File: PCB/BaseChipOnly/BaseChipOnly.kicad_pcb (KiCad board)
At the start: 2 copper layers, 39.1 x 68.8 mm, 31 parts, among them J1 Barrel_Jack_Connector, J2 Morsetto, J3 ESP32_PROG_1x6, U1 ESP32-WROOM-32U, U4 LM2596S-ADJ

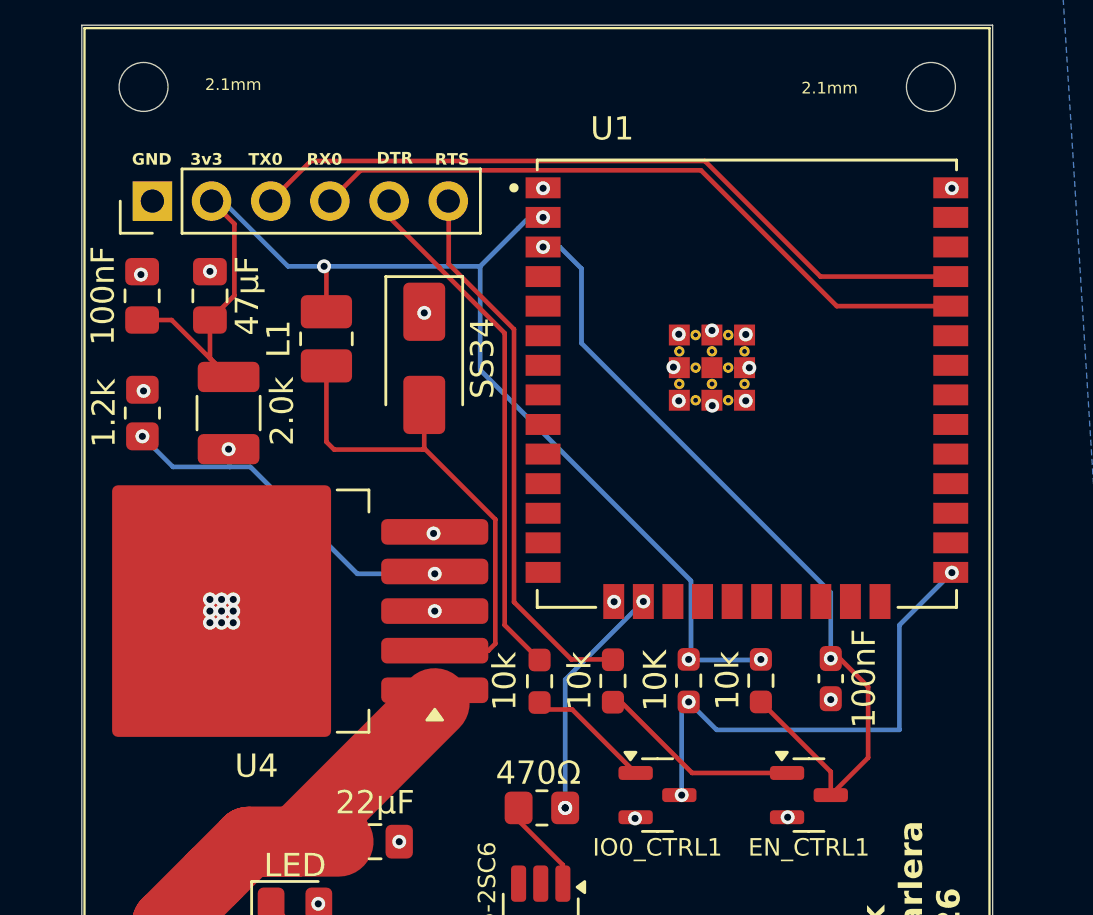
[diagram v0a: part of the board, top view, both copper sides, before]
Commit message: chore: update 3D models and PCB layout
Replace vaso/tappo STLs with new revisions (BaseVaso, Foglia, TasselloFissaggioPCB, VasoGiusto); minor kicad_pcb update.

Co-Authored-By: Claude Sonnet 5 <noreply@anthropic.com>
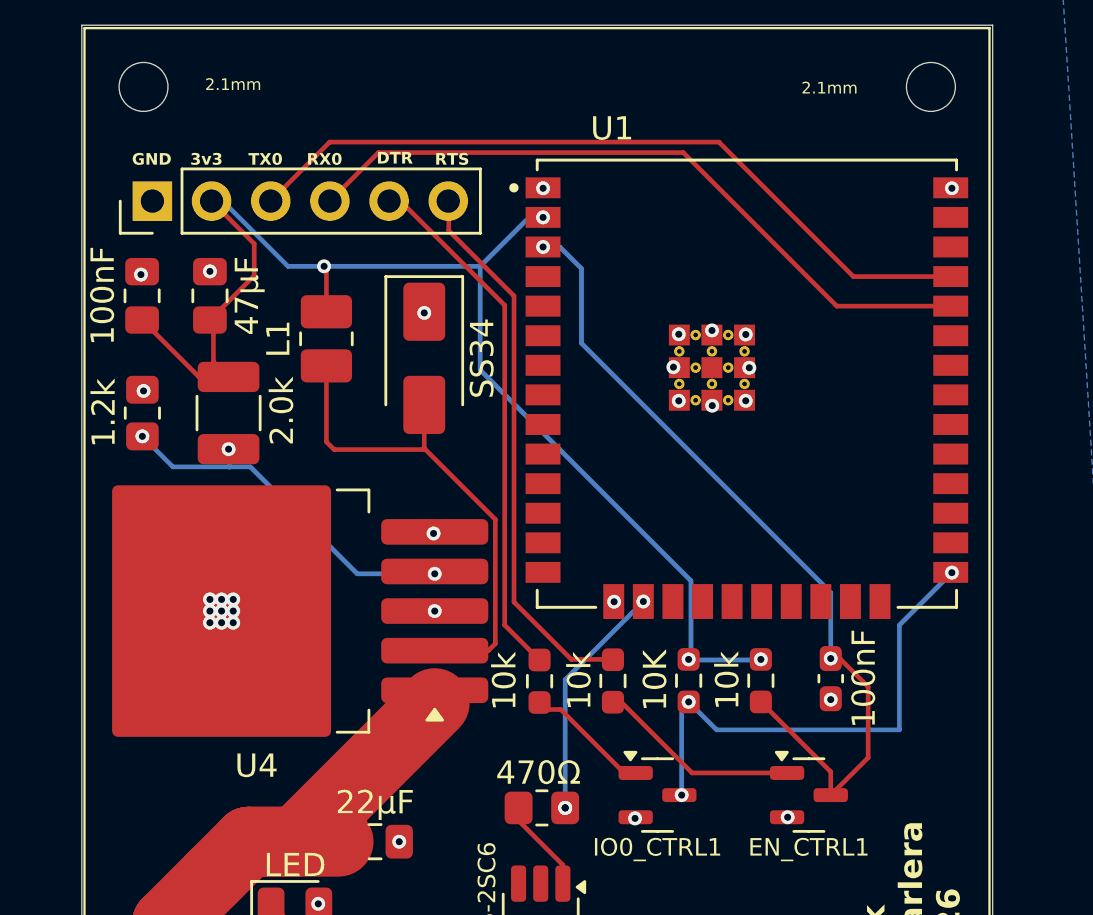
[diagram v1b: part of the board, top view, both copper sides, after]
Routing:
- net +3V3: track 55.6 -> 56.3 mm
- net Net-(J3-TX0): track 32.0 -> 32.6 mm
- net Net-(J3-RX0): track 29.6 -> 30.2 mm
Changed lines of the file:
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@@
 	(segment
 		(start 135.05 50.332323)
-		(end 134.25 49.532323)
-		(width 0.2)
-		(layer "F.Cu")
-		(net 3)
-	)
-	(segment
-		(start 135.3 43.762323)
-		(end 134.32 42.782323)
+		(end 134.400625 49.682948)
+		(width 0.2)
+		(layer "F.Cu")
+		(net 3)
+	)
+	(segment
+		(start 134.400625 48.038125)
+		(end 134.25 47.8875)
 		(width 0.2)
 		(layer "F.Cu")
@@
 	)
 	(segment
+		(start 134.25 47.8875)
+		(end 136.15 45.9875)
+		(width 0.2)
+		(layer "F.Cu")
+		(net 3)
+	)
+	(segment
 		(start 139.25 45.682323)
 		(end 139.15 45.582323)
@@
 	)
 	(segment
+		(start 134.400625 49.682948)
+		(end 134.400625 48.038125)
+		(width 0.2)
+		(layer "F.Cu")
+		(net 3)
+	)
+	(segment
+		(start 136.15 44.612323)
+		(end 134.32 42.782323)
+		(width 0.2)
+		(layer "F.Cu")
+		(net 3)
+	)
+	(segment
 		(start 154.9 62.457323)
 		(end 154.8 62.457323)
@@
 	)
 	(segment
+		(start 136.15 45.9875)
+		(end 136.15 44.612323)
+		(width 0.2)
+		(layer "F.Cu")
+		(net 3)
+	)
+	(segment
+		(start 133.782323 50.332323)
+		(end 131.3375 47.8875)
+		(width 0.2)
+		(layer "F.Cu")
+		(net 3)
+	)
+	(segment
 		(start 135.05 50.332323)
-		(end 132.605177 47.8875)
-		(width 0.2)
-		(layer "F.Cu")
-		(net 3)
-	)
-	(segment
-		(start 135.3 46.8375)
-		(end 135.3 43.762323)
-		(width 0.2)
-		(layer "F.Cu")
-		(net 3)
-	)
-	(segment
-		(start 134.25 49.532323)
-		(end 134.25 47.8875)
-		(width 0.2)
-		(layer "F.Cu")
-		(net 3)
-	)
-	(segment
-		(start 134.25 47.8875)
-		(end 135.3 46.8375)
+		(end 133.782323 50.332323)
 		(width 0.2)
 		(layer "F.Cu")
@@
 		(net 3)
 	)
-	(segment
-		(start 132.605177 47.8875)
-		(end 131.3375 47.8875)
-		(width 0.2)
-		(layer "F.Cu")
-		(net 3)
-	)
 	(via
 		(at 154.8 62.457323)
@@
 	)
 	(segment
+		(start 152.032323 67.332323)
+		(end 152.525 67.332323)
+		(width 0.2)
+		(layer "F.Cu")
+		(net 7)
+	)
+	(segment
+		(start 149.307323 64.607323)
+		(end 152.032323 67.332323)
+		(width 0.2)
+		(layer "F.Cu")
+		(net 7)
+	)
+	(segment
 		(start 148.4 64.607323)
-		(end 149.8 64.607323)
-		(width 0.2)
-		(layer "F.Cu")
-		(net 7)
-	)
-	(segment
-		(start 149.8 64.607323)
-		(end 152.525 67.332323)
+		(end 149.307323 64.607323)
 		(width 0.2)
 		(layer "F.Cu")
@@
 	)
 	(segment
-		(start 147.303 48.285323)
-		(end 144.5 45.482323)
+		(start 147.303 46.853)
+		(end 144.5 44.05)
 		(width 0.2)
 		(layer "F.Cu")
@@
 	)
 	(segment
-		(start 144.5 45.482323)
-		(end 144.5 42.802323)
+		(start 144.5 42.802323)
+		(end 144.48 42.782323)
+		(width 0.2)
+		(layer "F.Cu")
+		(net 11)
+	)
+	(segment
+		(start 151.9 62.457323)
+		(end 149.763 62.457323)
 		(width 0.2)
 		(layer "F.Cu")
@@
 	)
 	(segment
+		(start 144.5 44.05)
+		(end 144.5 42.802323)
+		(width 0.2)
+		(layer "F.Cu")
+		(net 11)
+	)
+	(segment
 		(start 147.303 59.997323)
-		(end 147.303 48.285323)
+		(end 147.303 46.853)
 		(width 0.2)
 		(layer "F.Cu")
 		(net 11)
-	)
-	(segment
-		(start 144.5 42.802323)
-		(end 144.48 42.782323)
-		(width 0.2)
-		(layer "F.Cu")
-		(net 11)
-	)
-	(segment
-		(start 151.9 62.457323)
-		(end 149.763 62.457323)
-		(width 0.2)
-		(layer "F.Cu")
-		(net 11)
-	)
-	(segment
-		(start 146.902 60.984323)
-		(end 146.902 48.451423)
-		(width 0.2)
-		(layer "F.Cu")
-		(net 12)
-	)
-	(segment
-		(start 146.902 48.451423)
-		(end 144.099 45.648423)
-		(width 0.2)
-		(layer "F.Cu")
-		(net 12)
 	)
 	(segment
@@
 	)
 	(segment
-		(start 141.94 43.472323)
+		(start 146.902 47.252)
+		(end 142.432323 42.782323)
+		(width 0.2)
+		(layer "F.Cu")
+		(net 12)
+	)
+	(segment
+		(start 142.432323 42.782323)
 		(end 141.94 42.782323)
 		(width 0.2)
@@
 	)
 	(segment
-		(start 144.099 45.631323)
-		(end 141.94 43.472323)
-		(width 0.2)
-		(layer "F.Cu")
-		(net 12)
-	)
-	(segment
-		(start 144.099 45.648423)
-		(end 144.099 45.631323)
+		(start 146.902 60.984323)
+		(end 146.902 47.252)
 		(width 0.2)
 		(layer "F.Cu")
@@
 	)
 	(segment
-		(start 140.721 41.461323)
-		(end 155.329 41.461323)
+		(start 141.482323 40.7)
+		(end 154.567677 40.7)
+		(width 0.2)
+		(layer "F.Cu")
+		(net 49)
+	)
+	(segment
+		(start 154.567677 40.7)
+		(end 161.16 47.292323)
 		(width 0.2)
 		(layer "F.Cu")
@@
 	(segment
 		(start 139.4 42.782323)
-		(end 140.721 41.461323)
+		(end 141.482323 40.7)
 		(width 0.2)
 		(layer "F.Cu")
@@
 	)
 	(segment
-		(start 155.329 41.461323)
-		(end 161.16 47.292323)
-		(width 0.2)
-		(layer "F.Cu")
-		(net 49)
-	)
-	(segment
-		(start 155.4951 41.060323)
-		(end 160.4571 46.022323)
+		(start 156.1 40.25)
+		(end 161.872323 46.022323)
 		(width 0.2)
 		(layer "F.Cu")
@@
 	)
 	(segment
-		(start 138.582 41.060323)
-		(end 155.4951 41.060323)
+		(start 161.872323 46.022323)
+		(end 166.05 46.022323)
 		(width 0.2)
 		(layer "F.Cu")
@@
 	)
 	(segment
-		(start 160.4571 46.022323)
-		(end 166.05 46.022323)
+		(start 136.86 42.782323)
+		(end 139.392323 40.25)
 		(width 0.2)
 		(layer "F.Cu")
@@
 	)
 	(segment
-		(start 136.86 42.782323)
-		(end 138.582 41.060323)
-		(width 0.2)
-		(layer "F.Cu")
+		(start 139.392323 40.25)
+		(end 156.1 40.25)
+		(width 0.2)
+		(layer "F.Cu")
